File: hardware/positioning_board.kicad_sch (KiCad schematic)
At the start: 45 parts, among them J1 4P4C, J2 USB_C_Receptacle_USB2.0_16P, J3 Conn_01x04, J4 Conn_01x05, J5 Conn_01x05, Q1 MMBT3904, Q2 MMBT3904, SW1 SW_Push, SW2 SW_Push, U1 SN65HVD1782DR, U2 CH340K, U3 ESP32-S3-WROOM-1, U4 LSM6DS3, U5 TPS563200, U7 AMS1117-3.3

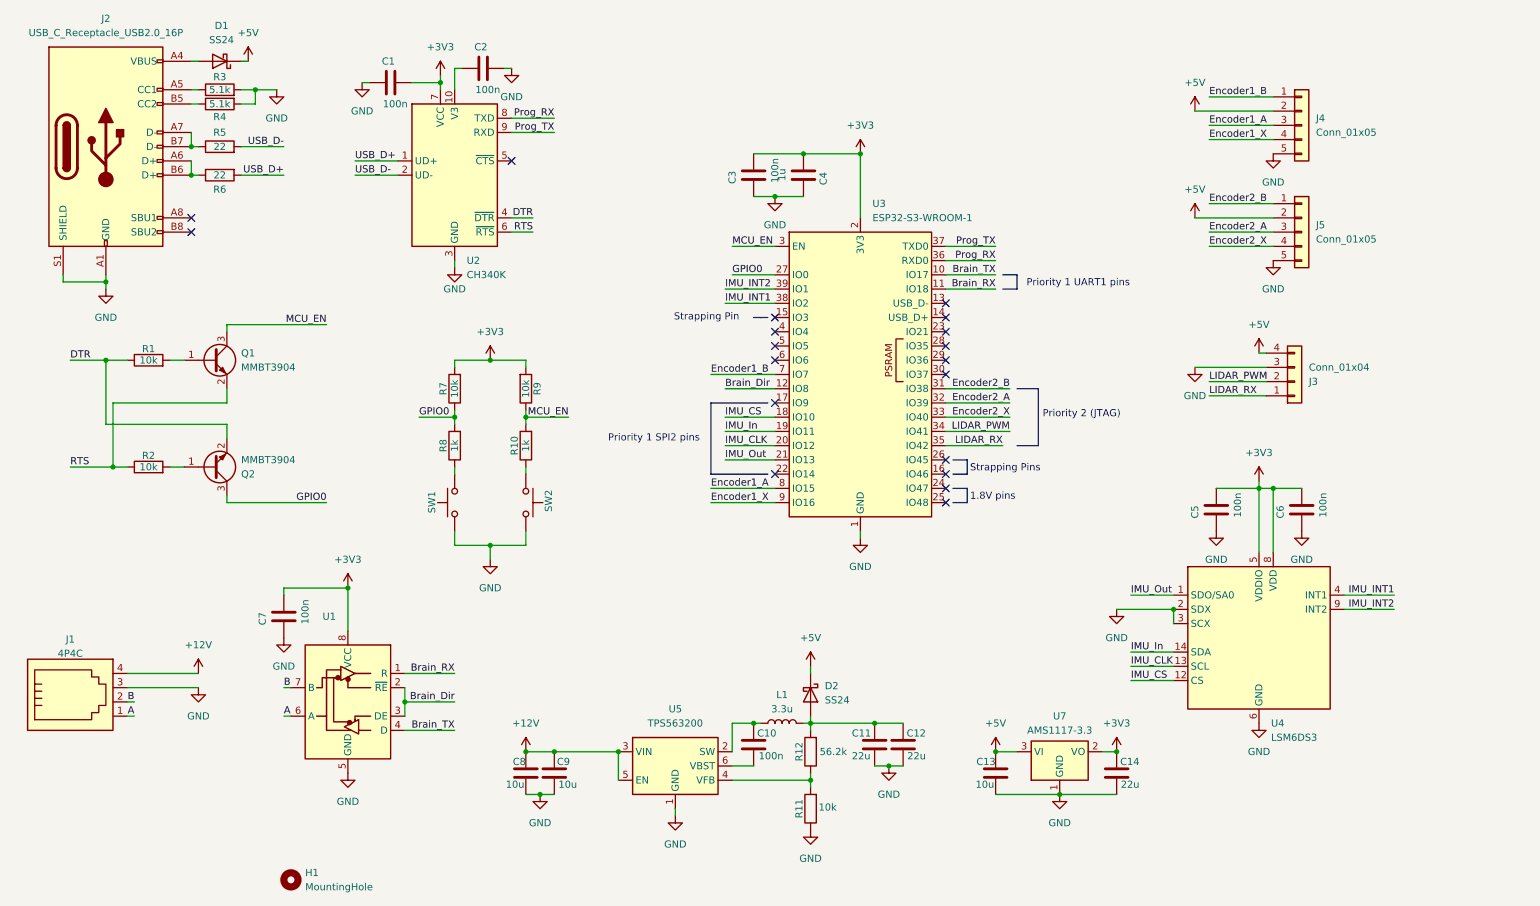
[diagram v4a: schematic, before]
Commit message: refactor into sub sheets
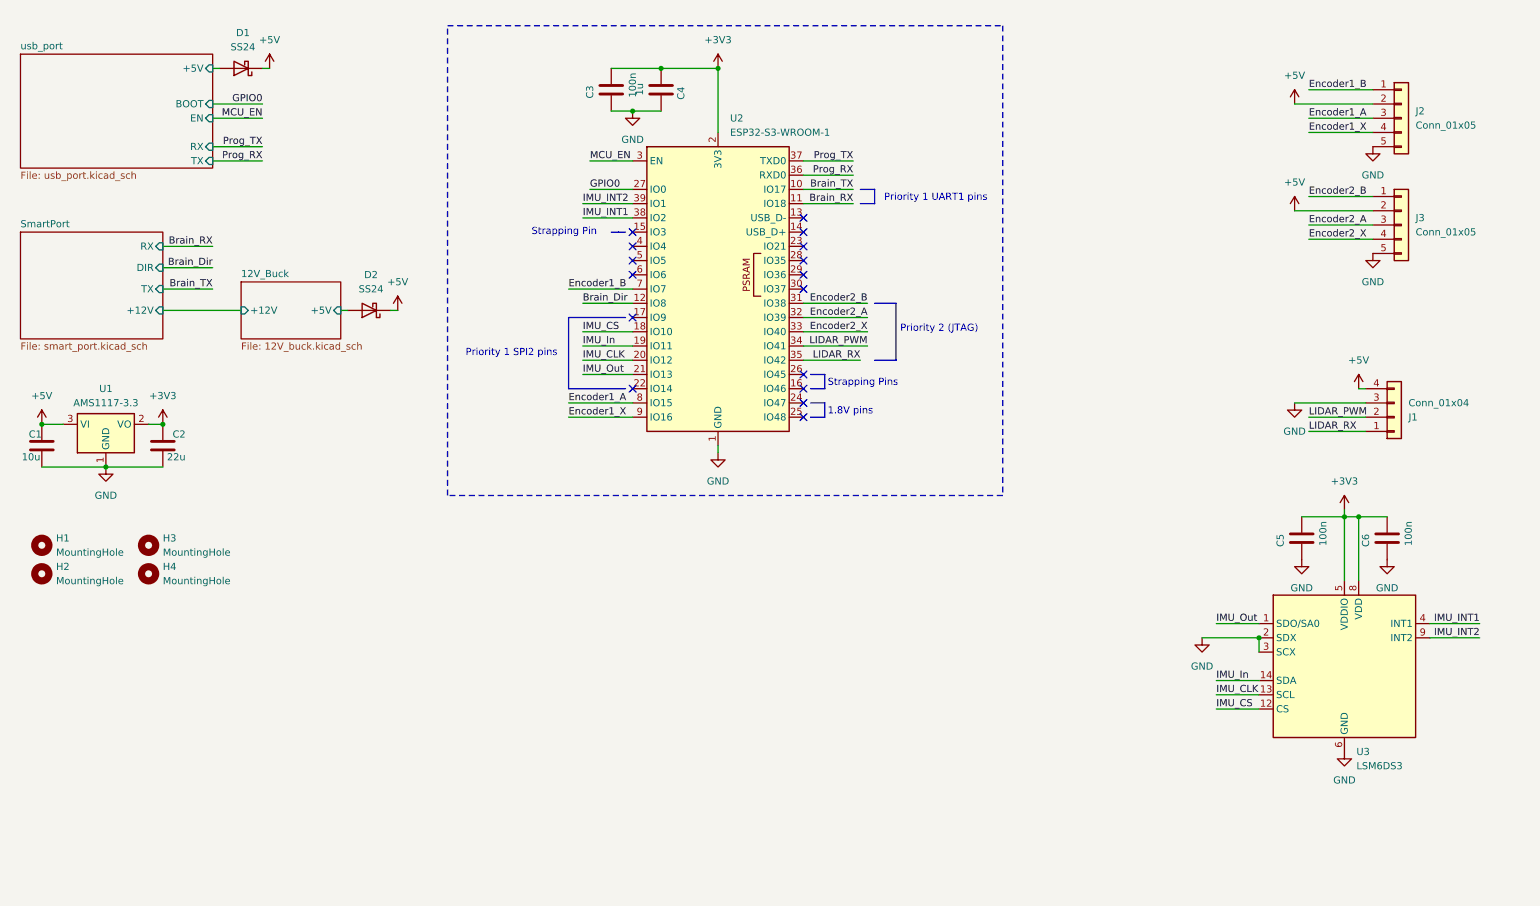
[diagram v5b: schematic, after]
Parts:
- removed C1, C10, C2, C7: 100n, Capacitor_SMD:C_0603_1608Metric, symbol Device:C
- removed C11, C12: 22u, Capacitor_SMD:C_0603_1608Metric, symbol Device:C
- removed C8, C9: 10u, Capacitor_SMD:C_0603_1608Metric, symbol Device:C
- removed J1: 4P4C, RJ11:RJ11-4P4C, symbol Connector:4P4C
- removed J2: USB_C_Receptacle_USB2.0_16P, Connector_USB:USB_C_Receptacle_GCT_USB4105-xx-A_16P_TopMnt_Horizontal, symbol Connector:USB_C_Receptacle_USB2.0_16P
- removed L1: 3.3u, Inductor_SMD:L_Changjiang_FXL0630, symbol Device:L
- removed Q1, Q2: MMBT3904, Package_TO_SOT_SMD:SOT-23, symbol Transistor_BJT:MMBT3904
- removed R1, R11, R2, R7, R9: 10k, Resistor_SMD:R_0603_1608Metric, symbol Device:R
- removed R10, R8: 1k, Resistor_SMD:R_0603_1608Metric, symbol Device:R
- removed R12: 56.2k, Resistor_SMD:R_0603_1608Metric, symbol Device:R
- removed R3, R4: 5.1k, Resistor_SMD:R_0603_1608Metric, symbol Device:R
- removed R5, R6: 22, Resistor_SMD:R_0603_1608Metric, symbol Device:R
- removed SW1, SW2: SW_Push, Button_Switch_SMD:SW_SPST_TS-1088-xR020, symbol Switch:SW_Push
- removed U1: SN65HVD1782DR, Package_SO:SOIC-8_3.9x4.9mm_P1.27mm, symbol Interface_UART:SN65HVD11HD
- removed U2: CH340K, Package_SO:SSOP-10-1EP_3.9x4.9mm_P1mm_EP2.1x3.3mm, symbol Interface_USB:CH340K
- removed U5: TPS563200, Package_TO_SOT_SMD:SOT-23-6, symbol Regulator_Switching:TPS563200
- added H2, H3, H4: MountingHole, MountingHole:MountingHole_4.3mm_M4, symbol Mechanical:MountingHole
- H1: footprint MountingHole:MountingHole_3.2mm_M3 -> MountingHole:MountingHole_4.3mm_M4
- renumbered C13 to C1, C14 to C2, J3 to J1, J4 to J2, J5 to J3, U7 to U1, U3 to U2, U4 to U3
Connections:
- net usb_port/+5V: now reaches D1.2 (A)
- net 12V_Buck/+5V: now reaches D2.2 (A)
- no-connect marks 19 -> 16
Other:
- added sheet 12V_Buck (12V_buck.kicad_sch)
- added sheet SmartPort (smart_port.kicad_sch)
- added sheet usb_port (usb_port.kicad_sch)
- moved on the sheet: C1, C2, C3, C4, C5, C6, D1, D2, H1, J1, J2, J3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

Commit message: relayout board
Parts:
- removed H4: MountingHole, MountingHole:MountingHole_4.3mm_M4, symbol Mechanical:MountingHole
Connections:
- net IMU_INT1: now also U2.39 (IO1); no longer U2.38 (IO2)
- net IMU_INT2: now also U2.38 (IO2); no longer U2.39 (IO1)
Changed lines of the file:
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@@
+		)
+	)
+	(label "IMU_INT2"
+		(at 118.11 52.07 0)
+		(effects
+			(font
+				(size 1.27 1.27)
+			)
+			(justify left bottom)
 		)
 	)
@@
 		)
 	)
-	(label "IMU_INT2"
-		(at 118.11 49.53 0)
-		(effects
-			(font
-				(size 1.27 1.27)
-			)
-			(justify left bottom)
-		)
-	)
 	(label "Brain_Dir"
 		(at 118.11 67.31 0)
@@
 		)
 	)
+	(label "IMU_INT1"
+		(at 118.11 49.53 0)
+		(effects
+			(font
+				(size 1.27 1.27)
+			)
+			(justify left bottom)
+		)
+	)
 	(label "IMU_Out"
 		(at 118.11 80.01 0)
@@
 	(label "Encoder1_X"
 		(at 247.65 36.83 0)
-		(effects
-			(font
-				(size 1.27 1.27)
-			)
-			(justify left bottom)
-		)
-	)
-	(label "IMU_INT1"
-		(at 118.11 52.07 0)
 		(effects
 			(font
@@
 					(unit 1)
 				)
-			)
-		)
-	)
-	(symbol
-		(lib_id "Mechanical:MountingHole")
-		(at 40.64 115.57 0)
-		(unit 1)
-		(exclude_from_sim no)
-		(in_bom no)
-		(on_board yes)
-		(dnp no)
-		(fields_autoplaced yes)
-		(property "Reference" "H4"
-			(at 43.18 114.2999 0)
-			(effects
-				(font
-					(size 1.27 1.27)
-				)
-				(justify left)
-			)
-		)
-		(property "Value" "MountingHole"
-			(at 43.18 116.8399 0)
-			(effects
-				(font
-					(size 1.27 1.27)
-				)
-				(justify left)
-			)
-		)
-		(property "Footprint" "MountingHole:MountingHole_4.3mm_M4"
-			(at 40.64 115.57 0)
-			(effects
-				(font
-					(size 1.27 1.27)
-				)
-				(hide yes)
-			)
-		)
-		(property "Datasheet" "~"
-			(at 40.64 115.57 0)
-			(effects
-				(font
-					(size 1.27 1.27)
-				)
-				(hide yes)
-			)
-		)
-		(property "Description" "Mounting Hole without connection"
-			(at 40.64 115.57 0)
-			(effects
-				(font
-					(size 1.27 1.27)
-				)
-				(hide yes)
-			)
-		)
-		(instances
-			(project "positioning_board"
-				(path "/6f62fc68-1fd8-4b2d-94a6-50bf685a778b"
-					(reference "H4")
-					(unit 1)
-				)

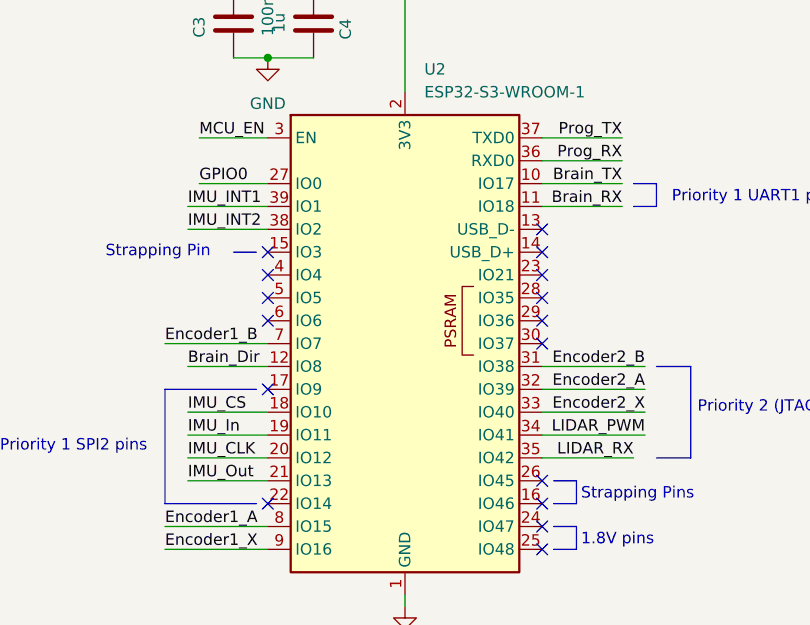
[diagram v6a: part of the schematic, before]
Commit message: swap lidar and brain UART channels
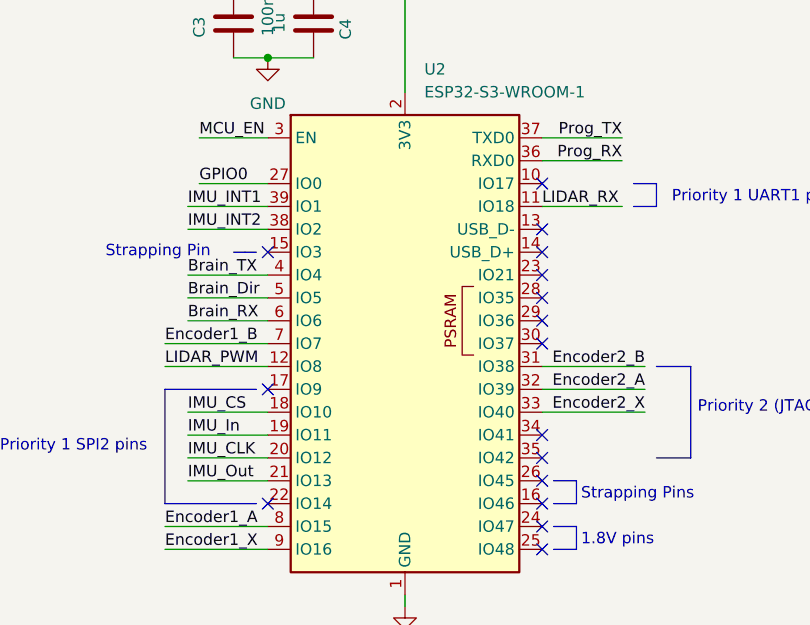
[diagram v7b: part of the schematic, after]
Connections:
- net Brain_Dir: now also U2.5 (IO5); no longer U2.12 (IO8)
- net Brain_RX: now also U2.6 (IO6); no longer U2.11 (IO18)
- net Brain_TX: now also U2.4 (IO4); no longer U2.10 (IO17)
- net LIDAR_PWM: now also U2.12 (IO8); no longer U2.34 (IO41)
- net LIDAR_RX: now also U2.11 (IO18); no longer U2.35 (IO42)
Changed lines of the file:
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@@
+	)
+	(no_connect
+		(at 157.48 46.99)
 	)
 	(no_connect
@@
 	)
 	(no_connect
-		(at 127 62.23)
-	)
-	(no_connect
-		(at 127 59.69)
-	)
-	(no_connect
 		(at 157.48 85.09)
 	)
@@
 	)
 	(no_connect
+		(at 157.48 77.47)
+	)
+	(no_connect
 		(at 157.48 57.15)
 	)
@@
 	)
 	(no_connect
-		(at 127 57.15)
+		(at 157.48 74.93)
 	)
 	(no_connect
@@
 	(wire
 		(pts
+			(xy 118.11 62.23) (xy 127 62.23)
+		)
+		(stroke
+			(width 0)
+			(type default)
+		)
+	)
+	(wire
+		(pts
 			(xy 43.18 68.58) (xy 57.15 68.58)
 		)
@@
 		)
 	)
-	(wire
-		(pts
-			(xy 157.48 46.99) (xy 166.37 46.99)
-		)
-		(stroke
-			(width 0)
-			(type default)
-		)
-	)
 	(polyline
 		(pts
@@
 	(wire
 		(pts
+			(xy 166.37 49.53) (xy 157.48 49.53)
+		)
+		(stroke
+			(width 0)
+			(type default)
+		)
+	)
+	(wire
+		(pts
 			(xy 43.18 88.9) (xy 40.64 88.9)
 		)
@@
 	(wire
 		(pts
+			(xy 118.11 59.69) (xy 127 59.69)
+		)
+		(stroke
+			(width 0)
+			(type default)
+		)
+	)
+	(wire
+		(pts
 			(xy 60.96 31.75) (xy 52.07 31.75)
 		)
@@
 	(wire
 		(pts
-			(xy 118.11 67.31) (xy 127 67.31)
+			(xy 115.57 67.31) (xy 127 67.31)
 		)
 		(stroke
@@
 	(wire
 		(pts
-			(xy 168.91 74.93) (xy 157.48 74.93)
-		)
-		(stroke
-			(width 0)
-			(type default)
-		)
-	)
-	(wire
-		(pts
 			(xy 52.07 60.96) (xy 43.18 60.96)
 		)
@@
 	(wire
 		(pts
-			(xy 167.64 77.47) (xy 157.48 77.47)
+			(xy 118.11 57.15) (xy 127 57.15)
 		)
 		(stroke
@@
 	(wire
 		(pts
-			(xy 157.48 49.53) (xy 166.37 49.53)
-		)
-		(stroke
-			(width 0)
-			(type default)
-		)
-	)
-	(wire
-		(pts
 			(xy 245.11 85.09) (xy 257.81 85.09)
 		)
@@
 			(width 0)
 			(type default)
-		)
-	)
-	(label "Brain_TX"
-		(at 166.37 46.99 180)
-		(effects
-			(font
-				(size 1.27 1.27)
-			)
-			(justify right bottom)
 		)
 	)
@@
 		)
 	)
-	(label "LIDAR_PWM"
-		(at 168.91 74.93 180)
-		(effects
-			(font
-				(size 1.27 1.27)
-			)
-			(justify right bottom)
-		)
-	)
 	(label "Encoder1_X"
 		(at 115.57 87.63 0)
@@
 		)
 	)
-	(label "LIDAR_RX"
-		(at 167.64 77.47 180)
-		(effects
-			(font
-				(size 1.27 1.27)
-			)
-			(justify right bottom)
-		)
-	)
-	(label "Brain_Dir"
-		(at 118.11 67.31 0)
-		(effects
-			(font
-				(size 1.27 1.27)
-			)
-			(justify left bottom)
-		)
-	)
 	(label "Brain_Dir"
 		(at 52.07 60.96 180)
@@
 		)
 	)
-	(label "Brain_RX"
-		(at 166.37 49.53 180)
-		(effects
-			(font
-				(size 1.27 1.27)
-			)
-			(justify right bottom)
-		)
-	)
 	(label "IMU_In"
 		(at 118.11 74.93 0)
@@
 	)
 	(label "LIDAR_PWM"
+		(at 115.57 67.31 0)
+		(effects
+			(font
+				(size 1.27 1.27)
+			)
+			(justify left bottom)
+		)
+	)
+	(label "Brain_TX"
+		(at 118.11 57.15 0)
+		(effects
+			(font
+				(size 1.27 1.27)
+			)
+			(justify left bottom)
+		)
+	)
+	(label "LIDAR_PWM"
 		(at 247.65 87.63 0)
 		(effects
@@
 		)
 	)
+	(label "Brain_Dir"
+		(at 118.11 59.69 0)
+		(effects
+			(font
+				(size 1.27 1.27)
+			)
+			(justify left bottom)
+		)
+	)
+	(label "LIDAR_RX"
+		(at 157.48 49.53 0)
+		(effects
+			(font
+				(size 1.27 1.27)
+			)
+			(justify left bottom)
+		)
+	)
+	(label "Brain_RX"
+		(at 118.11 62.23 0)
+		(effects
+			(font
+				(size 1.27 1.27)
+			)
+			(justify left bottom)
+		)
+	)

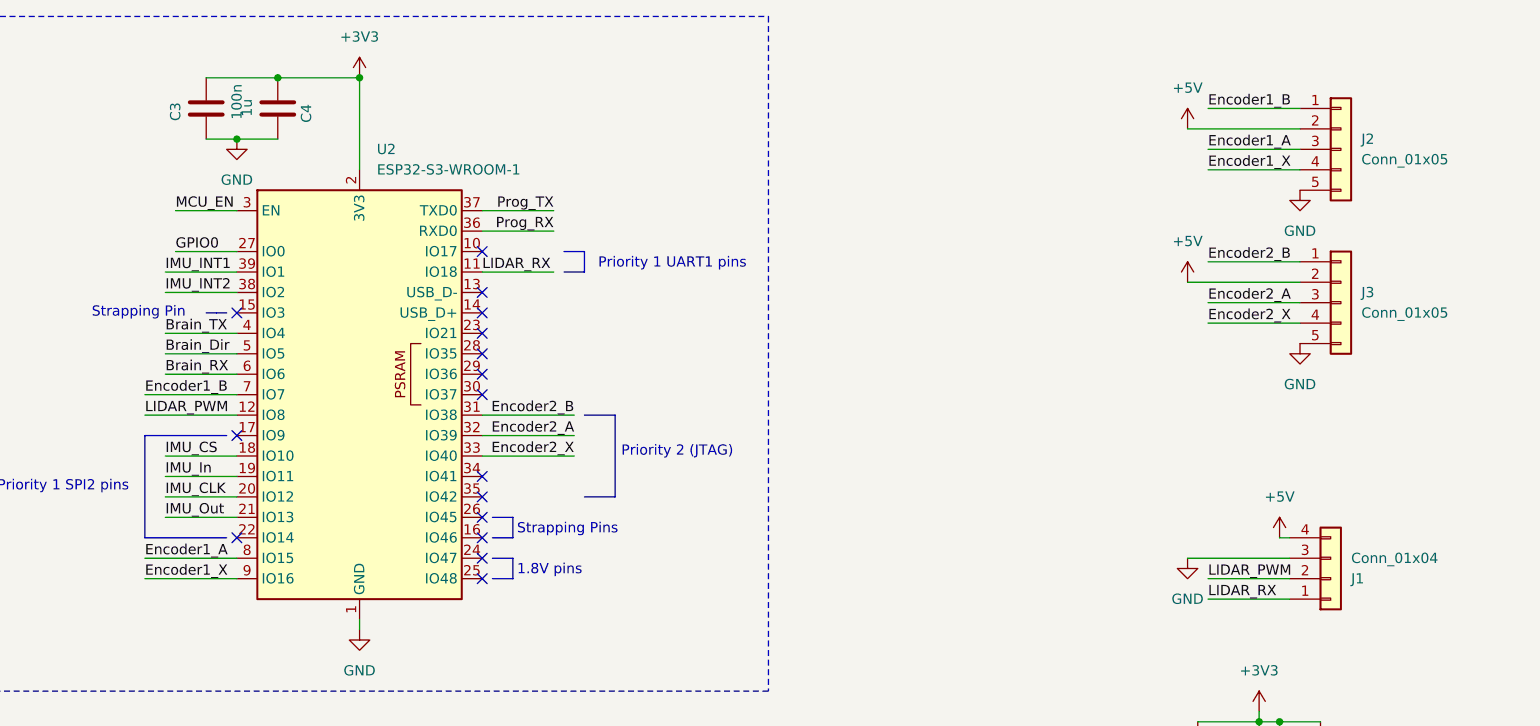
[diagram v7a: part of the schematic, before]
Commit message: add logic level shifters
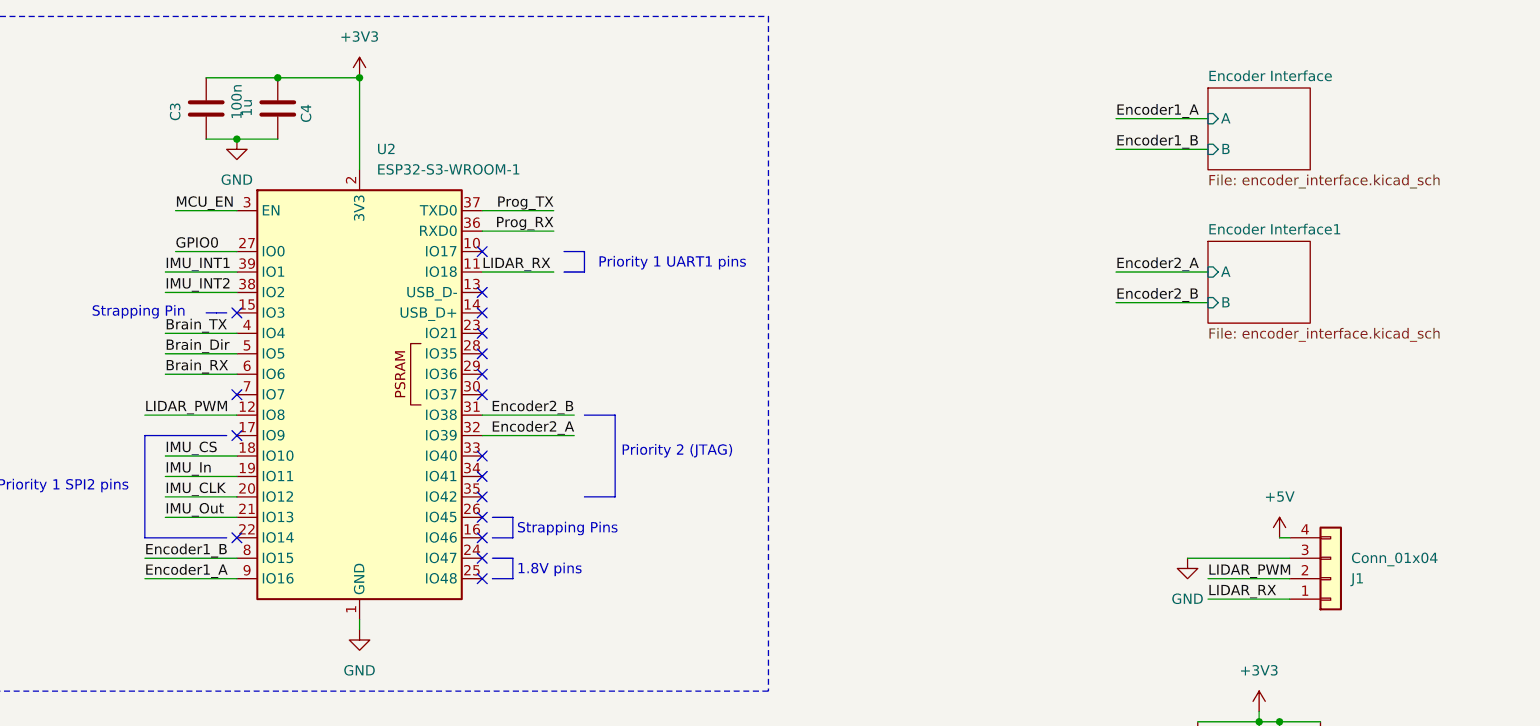
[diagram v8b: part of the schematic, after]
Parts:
- removed J2, J3: Conn_01x05, Connector_JST:JST_XH_S5B-XH-A_1x05_P2.50mm_Horizontal, symbol Connector_Generic:Conn_01x05
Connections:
- net Encoder1_X is gone; now on net Encoder1_A: U2.9 (IO16)
- net Encoder1_A: no longer U2.8 (IO15)
- net Encoder1_B: now also U2.8 (IO15); no longer U2.7 (IO7)
- net Encoder2_X: no longer names the net of U2.33 (IO40)
- no-connect marks 16 -> 18
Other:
- added sheet Encoder Interface (encoder_interface.kicad_sch)
- added sheet Encoder Interface1 (encoder_interface.kicad_sch)
